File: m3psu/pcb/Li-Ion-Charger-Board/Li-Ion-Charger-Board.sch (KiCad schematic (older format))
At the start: 43 parts

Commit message: Finished routing the Li-ion Charger board. Needs checking. Did a brief check of the MCU board. Not done yet.
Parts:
- IC2: renamed from IC?; footprint agg:HVQFN-16-NXP -> agg:QFN-16-EP-NXP
- J3: renamed from J?; footprint agg:SFML-105-02-L-D -> agg:TFML-105-02-L-D
- Q4: renamed from Q?; footprint agg:PowerFLAT5x6 -> agg:PowerFLAT-5x6
- Q6: renamed from Q?; footprint agg:PowerPair3x3 -> agg:PowerPair-3x3
- gave numbers to parts that had none: 37
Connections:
- wire segments 237 -> 234
- no-connect marks 1 -> 5

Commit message: Took away bottom north connector for MCU board, and top north connector for Li-ion board.
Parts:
- removed J3: NORTH TOP, agg:TFML-105-02-L-D, symbol CONN_02x05
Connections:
- wire segments 234 -> 224
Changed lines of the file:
@@
 $EndComp
-$Comp
-L CONN_02x05 J3
-U 1 1 56ECF1F6
-P 8950 3400
-F 0 "J3" H 8850 3500 50  0000 L CNN
-F 1 "NORTH TOP" H 8900 2900 50  0000 C CNN
-F 2 "agg:TFML-105-02-L-D" H 8950 3400 50  0001 C CNN
-F 3 "" H 8950 3400 50  0001 C CNN
-	1    8950 3400
-	1    0    0    -1
-$EndComp
-Wire Wire Line
-	8750 3400 8650 3400
-Wire Wire Line
-	8750 3500 8650 3500
-Wire Wire Line
-	8750 3600 8650 3600
-Wire Wire Line
-	8750 3700 8650 3700
-Wire Wire Line
-	8750 3800 8650 3800
-Wire Wire Line
-	9050 3400 9150 3400
-Wire Wire Line
-	9050 3500 9150 3500
-Wire Wire Line
-	9050 3600 9150 3600
-Wire Wire Line
-	9050 3700 9150 3700
-Text Label 8650 3400 2    60   ~ 0
-V_MAIN
-Text Label 9150 3400 0    60   ~ 0
-V_MAIN
-Text Label 8650 3700 2    60   ~ 0
-SDA
-Text Label 8650 3800 2    60   ~ 0
-SCL
-Text Label 8650 3500 2    60   ~ 0
-VBATT
-Text Label 9150 3600 0    60   ~ 0
-BATT1
-Text Label 9150 3500 0    60   ~ 0
-VBATT
-Text Label 8650 3600 2    60   ~ 0
-3v3_PSU
-Text Label 9150 3700 0    60   ~ 0
-BATT2
-Wire Wire Line
-	9050 3800 9150 3800
-Text Label 9150 3800 0    60   ~ 0
-~ALERT
 $Comp
 L CONN_02x05 J6

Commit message: Update M3PSU-charger schematic and board, generate and check gerbers.
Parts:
- added C10: 100n, agg:0402, symbol C
- added J3: TAP, agg:SIL-254P-01, symbol CONN_01x01
- added J7: BAT+, agg:SIL-254P-01, symbol CONN_01x01
- added J8: BAT-, agg:SIL-254P-01, symbol CONN_01x01
- Q1, Q3: symbol NFET -> NFET-RESCUE-Li-Ion-Charger-Board
- Q2, Q5: symbol PFET -> PFET-RESCUE-Li-Ion-Charger-Board
- R3: value 33k -> 10k; Farnell 2447160 -> 2447096
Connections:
- wire segments 224 -> 232

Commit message: Fix GDS issue in Li-Ion-Charger
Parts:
- Q1, Q3: symbol NFET-RESCUE-Li-Ion-Charger-Board -> NFET_GDS
- Q2, Q5: symbol PFET-RESCUE-Li-Ion-Charger-Board -> PFET_GDS
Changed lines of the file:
@@
 EESchema Schematic File Version 2
-LIBS:Li-Ion-Charger-Board-rescue
 LIBS:agg-kicad
 LIBS:Li-Ion-Charger-Board-cache
@@
 $EndComp
 $Comp
-L PFET-RESCUE-Li-Ion-Charger-Board Q5
+L PFET_GDS Q5
 U 1 1 56C79D18
 P 6650 2750
@@
 	4400 4150 4400 4200
 $Comp
-L PFET-RESCUE-Li-Ion-Charger-Board Q2
+L PFET_GDS Q2
 U 1 1 56DFD606
 P 5150 1650
@@
 $EndComp
 $Comp
-L NFET-RESCUE-Li-Ion-Charger-Board Q3
+L NFET_GDS Q3
 U 1 1 56E1C9CD
 P 5400 2150
@@
 $EndComp
 $Comp
-L NFET-RESCUE-Li-Ion-Charger-Board Q1
+L NFET_GDS Q1
 U 1 1 56E1CA5A
 P 4850 1900

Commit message: rebuild all PDFs from latest XMLs
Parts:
- Q2: footprint PowerPAK-1212-8 -> agg:PowerPAK-1212-8

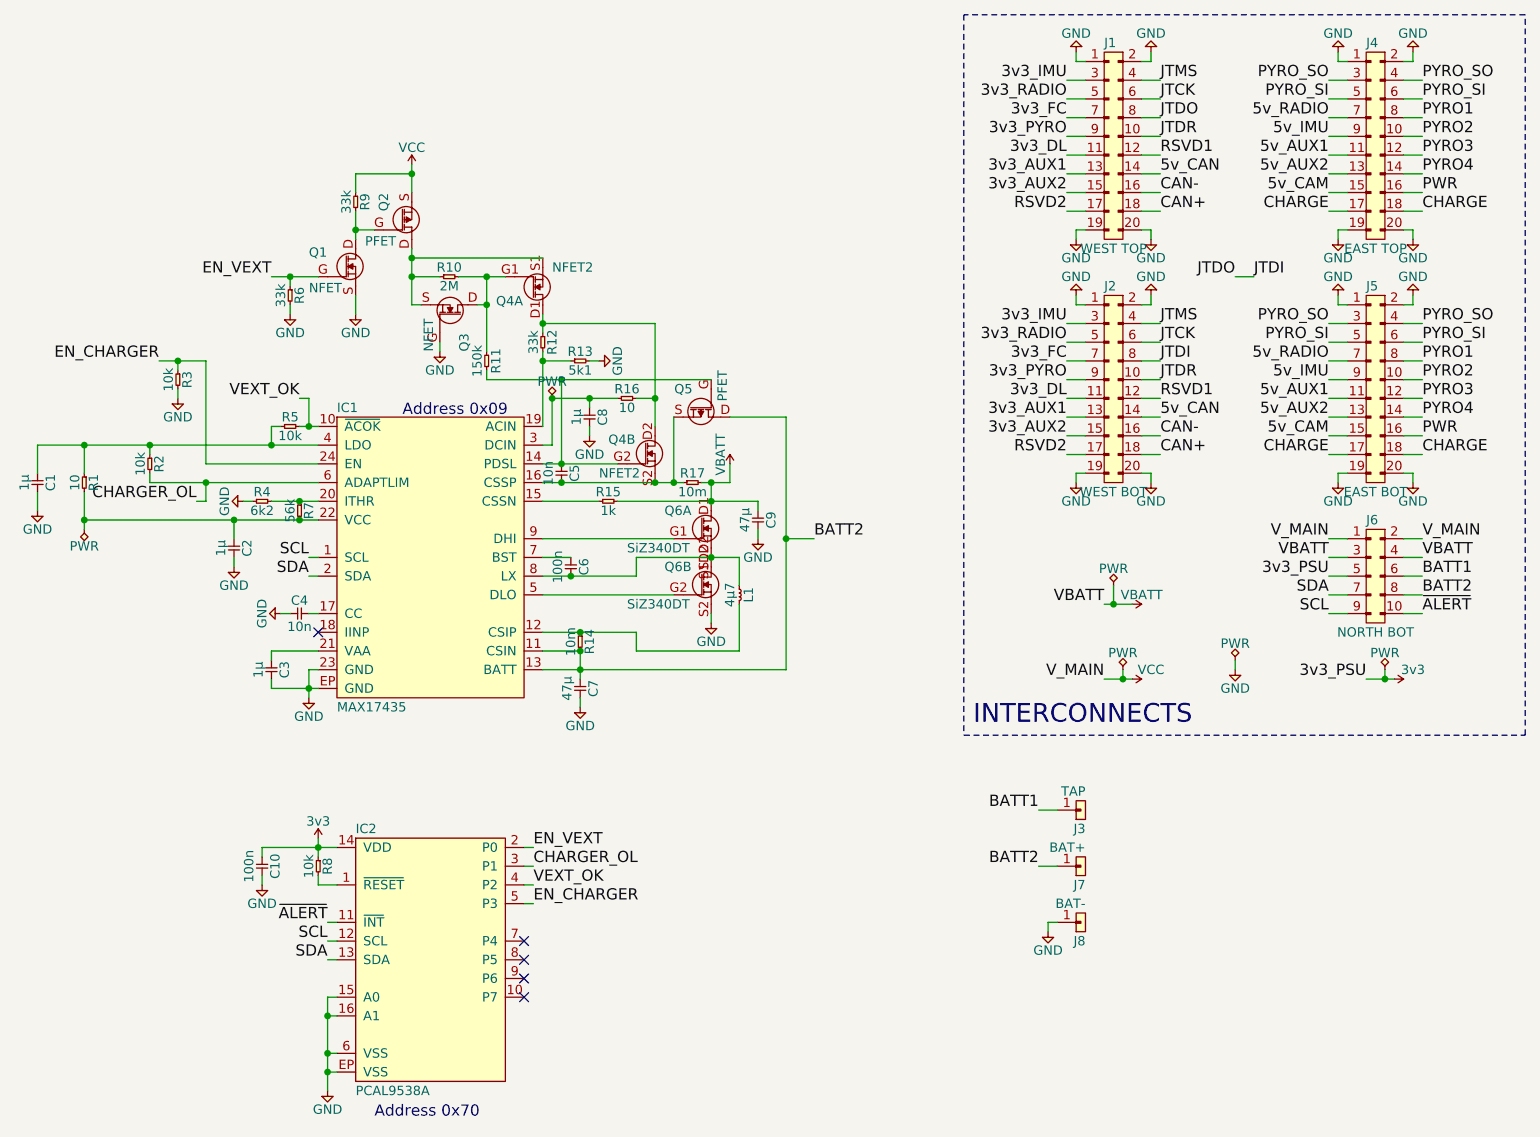
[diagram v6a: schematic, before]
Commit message: Connect charger input to VSHORE. Move battery tap pad for more clearance
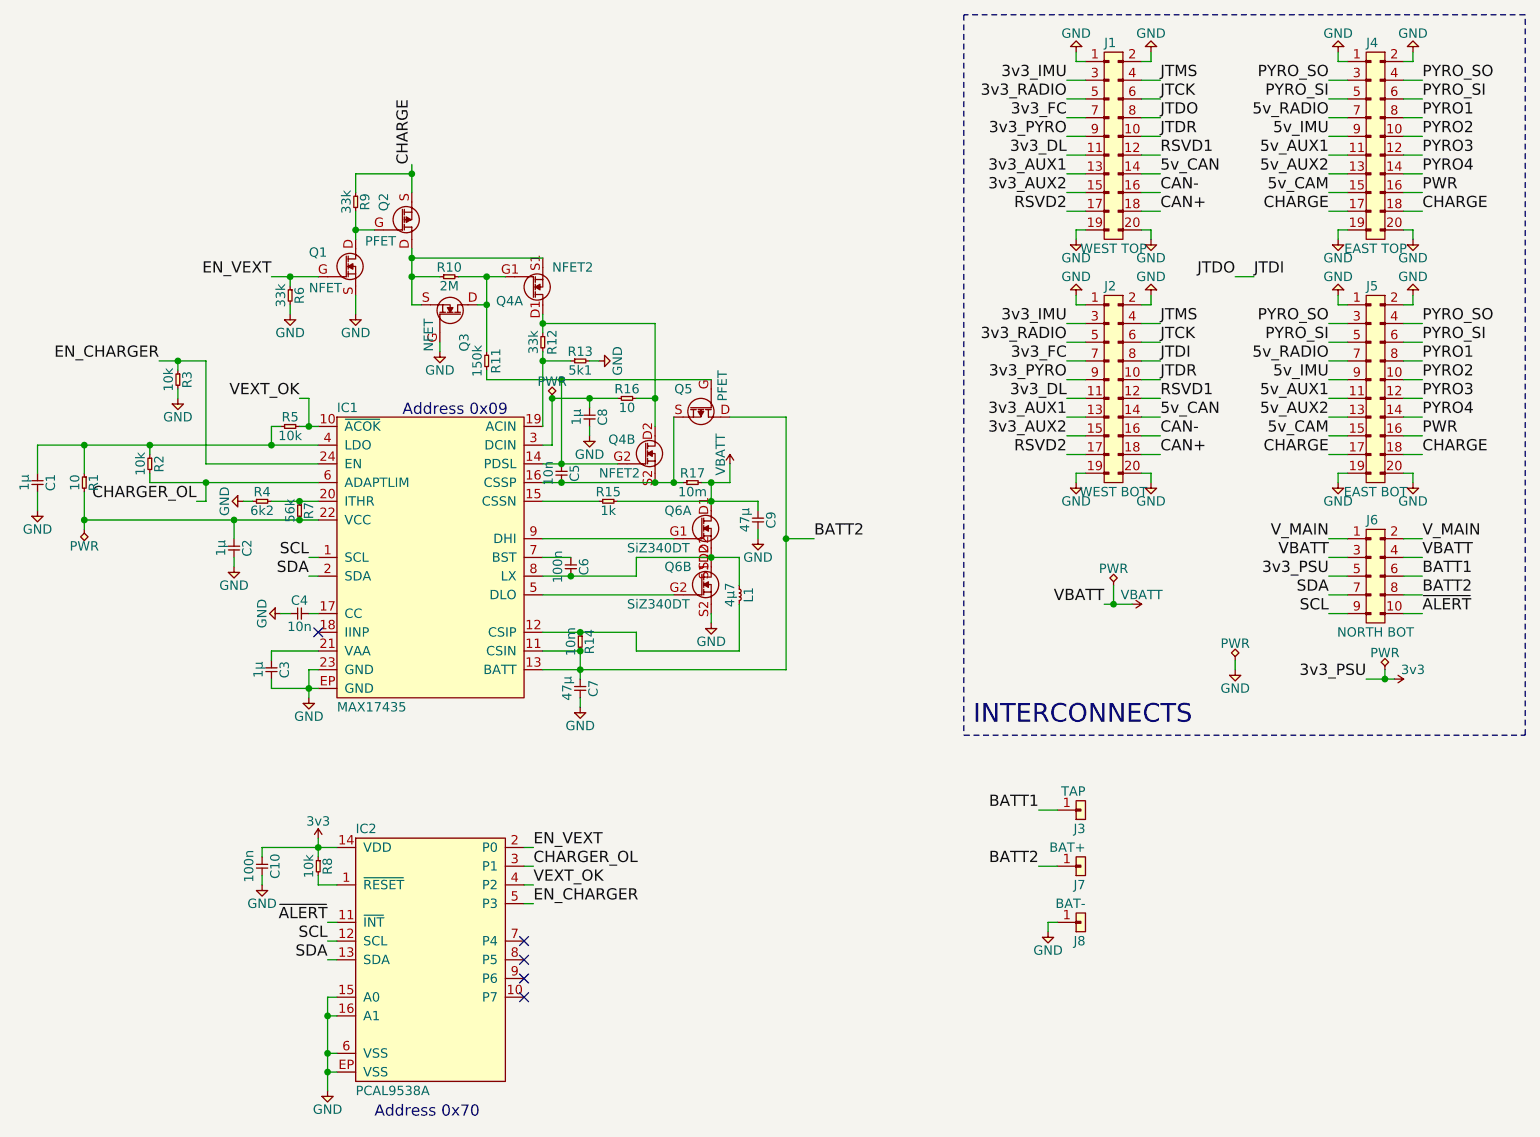
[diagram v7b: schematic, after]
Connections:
- net CHARGE: now also Q2.S, R9.1
- net VCC renamed V_MAIN
- net V_MAIN: no longer Q2.S, R9.1
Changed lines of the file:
@@
 LIBS:agg-kicad
 LIBS:Li-Ion-Charger-Board-cache
-EELAYER 25 0
+EELAYER 26 0
 EELAYER END
 $Descr A4 11693 8268
@@
 Address 0x09
 NoConn ~ 4650 3900
-$Comp
-L VCC #PWR012
-U 1 1 56E18C4B
-P 5150 1400
-F 0 "#PWR012" H 5150 1510 50  0001 L CNN
-F 1 "VCC" H 5150 1490 50  0000 C CNN
-F 2 "" H 5150 1400 60  0000 C CNN
-F 3 "" H 5150 1400 60  0000 C CNN
-	1    5150 1400
-	1    0    0    -1
-$EndComp
 $Comp
 L VBATT #PWR013
@@
 Text Label 10550 3800 0    60   ~ 0
 ~ALERT
-Text Label 8850 4150 2    60   ~ 0
-V_MAIN
-$Comp
-L VCC #PWR037
-U 1 1 56ED3312
-P 9000 4150
-F 0 "#PWR037" H 9000 4260 50  0001 L CNN
-F 1 "VCC" V 8950 4250 50  0000 C CNN
-F 2 "" H 9000 4150 60  0000 C CNN
-F 3 "" H 9000 4150 60  0000 C CNN
-	1    9000 4150
-	0    1    1    0
-$EndComp
-Wire Wire Line
-	8850 4150 9000 4150
 Text Label 4700 5450 2    60   ~ 0
 ~ALERT
@@
 3v3_PSU
 $Comp
-L PWR #FLG039
-U 1 1 56E4659E
-P 8950 4100
-F 0 "#FLG039" H 8950 4260 50  0001 C CNN
-F 1 "PWR" H 8950 4190 50  0000 C CNN
-F 2 "" H 8950 4100 50  0001 C CNN
-F 3 "" H 8950 4100 50  0001 C CNN
-	1    8950 4100
-	1    0    0    -1
-$EndComp
-Wire Wire Line
-	8950 4100 8950 4150
-Connection ~ 8950 4150
-$Comp
 L PWR #FLG040
 U 1 1 56E467CC
@@
 Wire Wire Line
 	8550 5450 8550 5500
+Text Label 5150 1400 1    60   ~ 0
+CHARGE
 $EndSCHEMATC

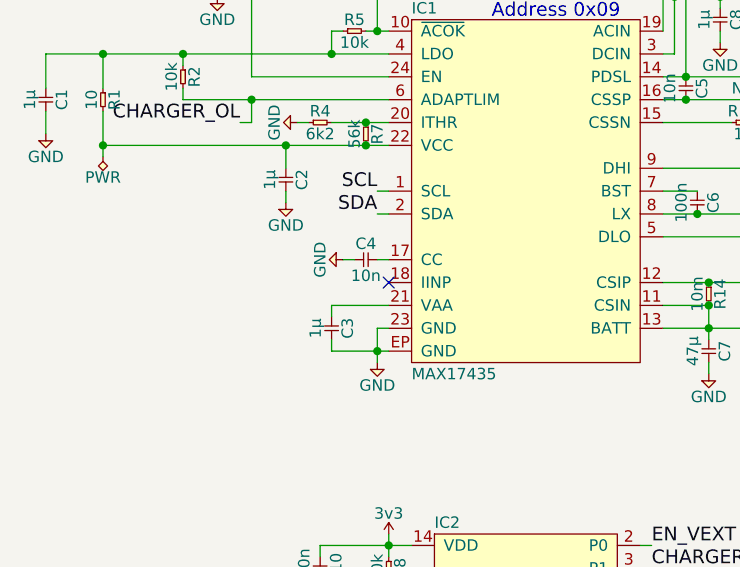
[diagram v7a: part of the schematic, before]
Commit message: Add IINP capacitor
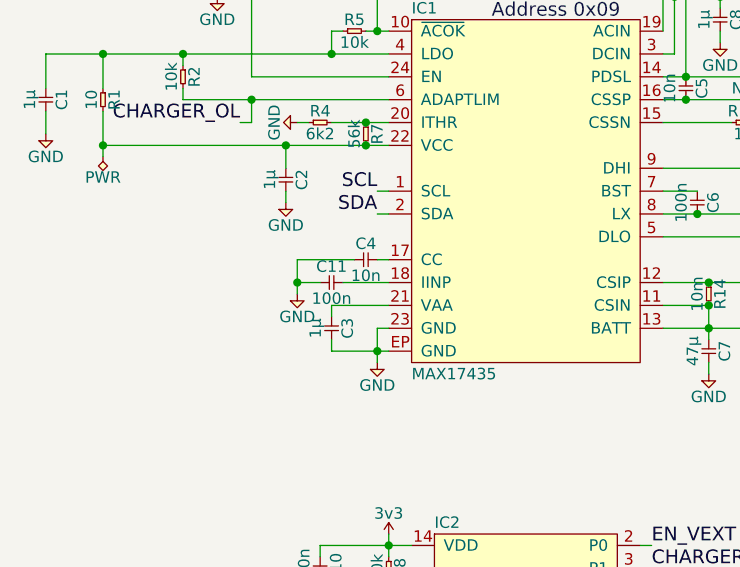
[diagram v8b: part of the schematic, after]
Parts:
- added C11: 100n, agg:0402, symbol C
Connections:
- net GND: now also C11.1
- net at IC1.18 (IINP): now also C11.2
- no-connect marks 5 -> 4
